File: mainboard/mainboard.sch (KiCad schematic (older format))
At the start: 107 parts, among them J1 USB_B_Micro, J2 Conn_01x19_MountingPin, J3 Conn_01x19_MountingPin, J4 Conn_01x02_Male, Q1 DMG2301L, Q2 MMBT3904, Q3 MMBT3904, SW1 SW_Push, SW2 SW_Push, U1 ESP32-WROOM-32, U2 tps63070, U3 tps63070, U4 tps63070, U5 CP2102N-A01-GQFN24, U6 BME680, U7 BH1750FVI, U8 LIS3MDL, U9 ADXL343

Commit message: Connect XT30 mounting pins to ground
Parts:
- removed J4: Conn_01x02_Male, mainboard:XT30PW, symbol Connector:Conn_01x02_Male
- added J?: Conn_01x02_MountingPin, mainboard:XT30PW, symbol Connector_Generic_MountingPin:Conn_01x02_MountingPin
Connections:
- wire segments 578 -> 582
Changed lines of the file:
@@
 Wire Wire Line
 	14550 4750 14550 4600
-$Comp
-L Connector:Conn_01x02_Male J4
-U 1 1 5DFAE882
-P 13750 4750
-F 0 "J4" H 13858 4931 50  0000 C CNN
-F 1 "Conn_01x02_Male" H 13858 4840 50  0000 C CNN
-F 2 "mainboard:XT30PW" H 13750 4750 50  0001 C CNN
-F 3 "~" H 13750 4750 50  0001 C CNN
-	1    13750 4750
-	1    0    0    -1
-$EndComp
 Wire Wire Line
 	13950 4750 14150 4750
@@
 	14550 5050 14550 4850
 Wire Wire Line
-	14550 4850 13950 4850
+	14550 4850 14000 4850
 Wire Notes Line
 	13450 3900 13450 5300
@@
 Wire Wire Line
 	8800 9500 8800 9100
-Wire Bus Line
-	8350 2150 8350 2500
-Wire Bus Line
-	9350 2500 9350 2750
 Connection ~ 8800 9100
 Wire Wire Line
@@
 	0    -1   -1   0
 $EndComp
+$Comp
+L Connector_Generic_MountingPin:Conn_01x02_MountingPin J?
+U 1 1 5F516B43
+P 13750 4750
+F 0 "J?" H 13672 4967 50  0000 C CNN
+F 1 "Conn_01x02_MountingPin" H 13672 4876 50  0000 C CNN
+F 2 "mainboard:XT30PW" H 13750 4750 50  0001 C CNN
+F 3 "~" H 13750 4750 50  0001 C CNN
+	1    13750 4750
+	-1   0    0    -1
+$EndComp
+Wire Wire Line
+	13750 5050 13750 5100
+Wire Wire Line
+	13750 5100 14000 5100
+Wire Wire Line
+	14000 5100 14000 4850
+Wire Bus Line
+	8350 2150 8350 2500
+Wire Bus Line
+	9350 2500 9350 2750
+Connection ~ 14000 4850
+Wire Wire Line
+	14000 4850 13950 4850
 $EndSCHEMATC

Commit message: Reassign silkscreen designators
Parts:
- gave numbers to parts that had none: 1
- renumbered C38 to C25, C39 to C26, C28 to C27, C29 to C28, C41 to C29, C42 to C32, C40 to C33, C44 to C34, C25 to C35, C43 to C36, C36 to C37, C37 to C38, C26 to C39, C27 to C40, C32 to C41, C33 to C42, C34 to C43, C35 to C44, D2 to D1, D1 to D2, F4 to F3, J2 to J3, J3 to J4, JP4 to JP1, R11 to R1, R8 to R10, R9 to R11, R10 to R12, R15 to R13, R16 to R14, R17 to R15, R18 to R16, R19 to R17, R20 to R18, R13 to R19, R12 to R2, R14 to R20, R1 to R3, R2 to R4, R3 to R5, R4 to R6, R5 to R7, R6 to R8, R7 to R9, U3 to U1, U4 to U3, U6 to U4, U8 to U5, U7 to U6, U5 to U7, U1 to U8

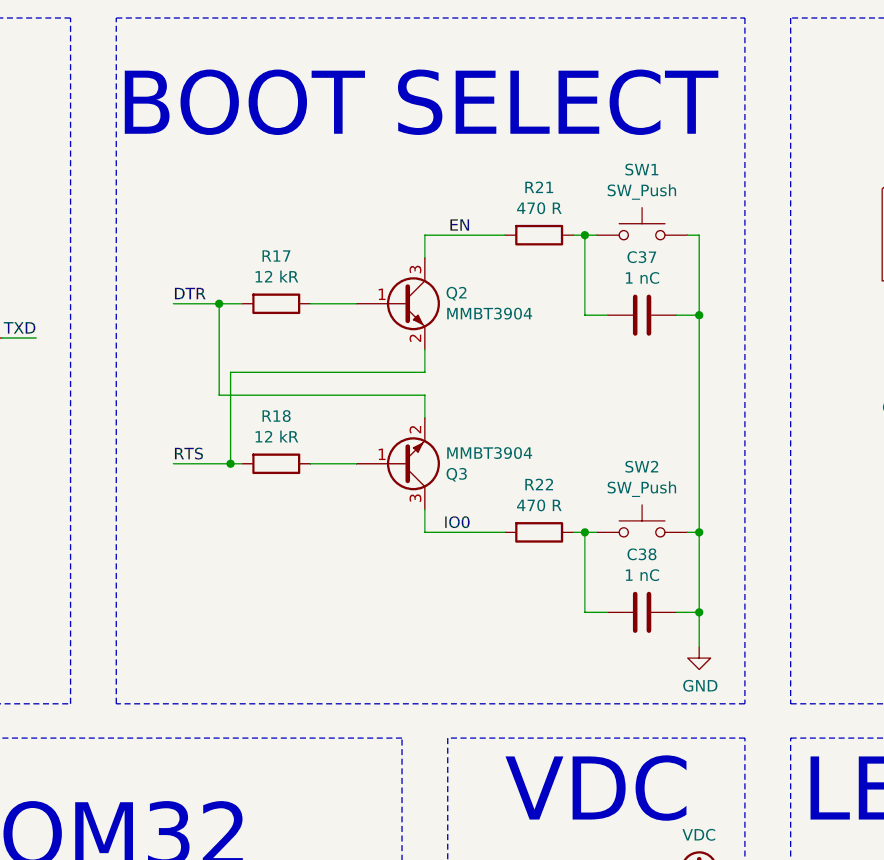
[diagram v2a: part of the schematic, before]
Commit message: Replace reset circuitry
It was the reference circuit used on the DevKitC V4 but it just plain does not work.
Replaced by much simpler and more reliable design.
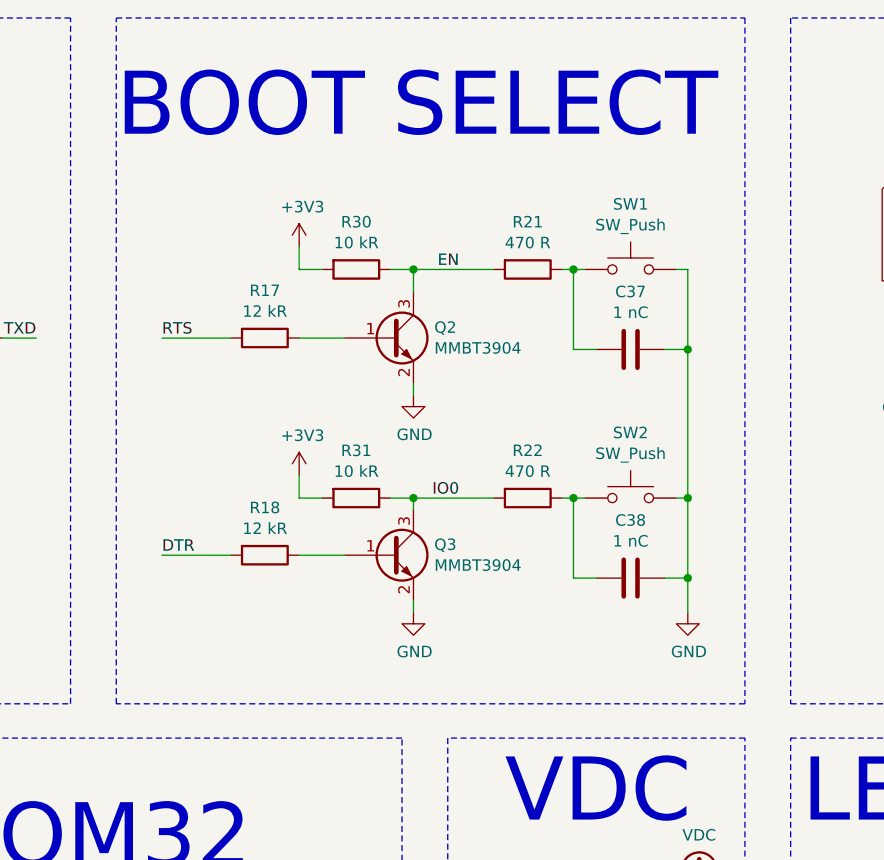
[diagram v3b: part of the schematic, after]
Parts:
- added R30, R31: 10 kR, Resistor_SMD:R_0805_2012Metric, symbol Device:R
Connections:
- net +3V3: now also R30.2, R31.2
- net DTR: now also R18.2; no longer Q3.2 (E), R17.2
- net EN: now also R30.1
- net GND: now also Q2.2 (E), Q3.2 (E)
- net IO0: now also R31.1
- net RTS: now also R17.2; no longer Q2.2 (E), R18.2
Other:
- moved on the sheet: C37, C38, Q2, Q3, R17, R18, R21, R22, SW1, SW2

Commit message: Revert "Replace reset circuitry"
This reverts commit 4aa51ba1305b71722c80cb68cdfb79191ae487c4.

CP2102N defaults to RTS + CTS high. Thus the reference reset circuitry is the only
simple way to make this work
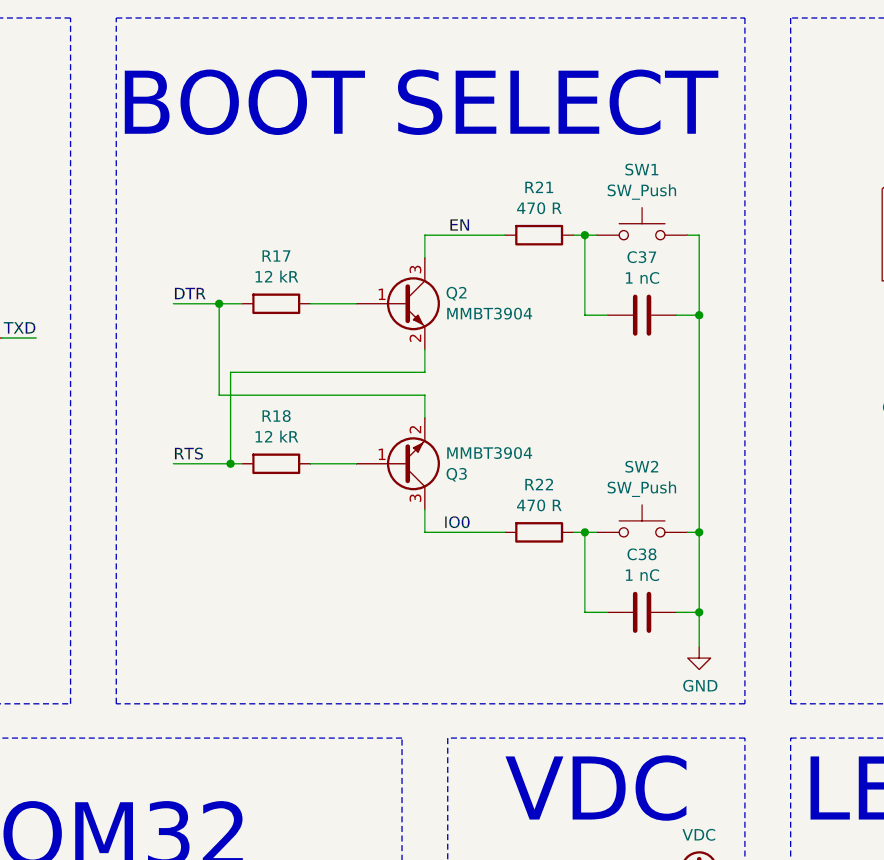
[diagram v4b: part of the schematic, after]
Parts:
- removed R30, R31: 10 kR, Resistor_SMD:R_0805_2012Metric, symbol Device:R
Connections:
- net DTR: now also Q3.2 (E), R17.2; no longer R18.2
- net GND: no longer Q2.2 (E), Q3.2 (E)
- net RTS: now also Q2.2 (E), R18.2; no longer R17.2
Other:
- moved on the sheet: C37, C38, Q2, Q3, R17, R18, R21, R22, SW1, SW2

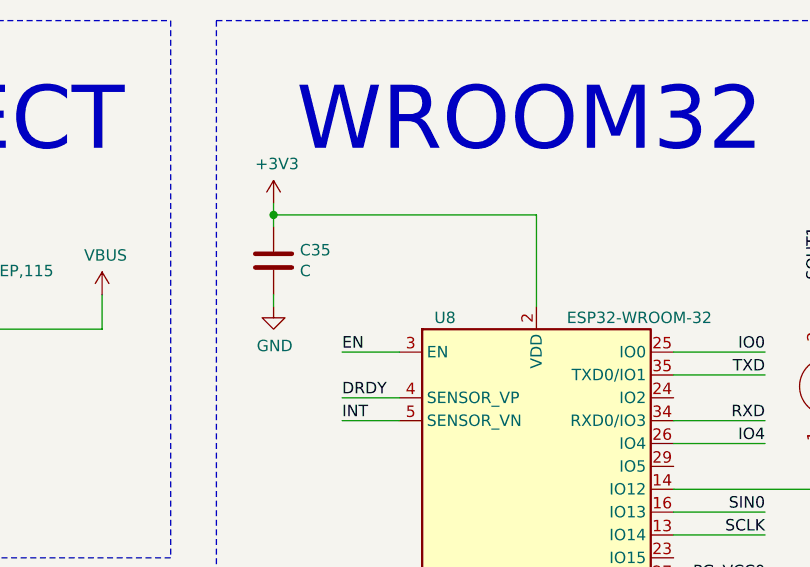
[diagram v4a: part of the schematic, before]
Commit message: Add ~RESET pullup
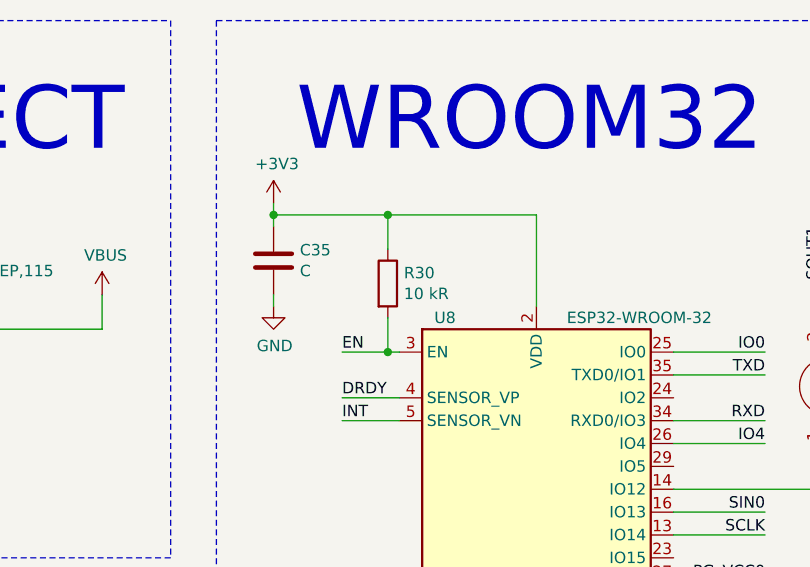
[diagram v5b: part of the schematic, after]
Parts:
- added R30: 10 kR, Resistor_SMD:R_0805_2012Metric, symbol Device:R
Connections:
- net +3V3: now also R30.1
- net EN: now also R30.2
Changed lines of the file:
@@
 $EndComp
-Wire Wire Line
-	14550 3500 14550 3350
-Connection ~ 14550 3350
 Wire Wire Line
 	14550 3000 14550 2050
@@
 	12250 2700 12500 2700
 Wire Wire Line
-	11000 5350 10750 5350
+	11000 5350 10950 5350
 Text Label 10750 5350 0    50   ~ 0
 EN
@@
 	11600 5150 11600 4750
 Wire Wire Line
-	11600 4750 10450 4750
+	11600 4750 10950 4750
 Connection ~ 10450 4750
 Wire Wire Line
@@
 Wire Wire Line
 	14000 5100 14000 4850
+Connection ~ 14000 4850
+Wire Wire Line
+	14000 4850 13950 4850
+Connection ~ 14550 3350
+Wire Wire Line
+	14550 3500 14550 3350
+$Comp
+L Device:R R30
+U 1 1 5D42A7B3
+P 10950 5050
+F 0 "R30" H 11020 5096 50  0000 L CNN
+F 1 "10 kR" H 11020 5005 50  0000 L CNN
+F 2 "Resistor_SMD:R_0805_2012Metric" V 10880 5050 50  0001 C CNN
+F 3 "~" H 10950 5050 50  0001 C CNN
+	1    10950 5050
+	1    0    0    -1
+$EndComp
+Wire Wire Line
+	10950 5200 10950 5350
+Connection ~ 10950 5350
+Wire Wire Line
+	10950 5350 10750 5350
+Wire Wire Line
+	10950 4900 10950 4750
 Wire Bus Line
 	8350 2150 8350 2500
 Wire Bus Line
 	9350 2500 9350 2750
-Connection ~ 14000 4850
-Wire Wire Line
-	14000 4850 13950 4850
+Connection ~ 10950 4750
+Wire Wire Line
+	10950 4750 10450 4750
 $EndSCHEMATC

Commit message: Add WROOM-32 with GND pad
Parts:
- U8: symbol RF_Module:ESP32-WROOM-32 -> esp32-wroom-32_gnd_pad:ESP32-WROOM-32
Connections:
- net GND: now also U8.39 (GND)
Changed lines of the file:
@@
 $EndDescr
 $Comp
-L RF_Module:ESP32-WROOM-32 U8
+L esp32-wroom-32_gnd_pad:ESP32-WROOM-32 U8
 U 1 1 5CF907D7
 P 11600 6550
@@
 Wire Wire Line
 	10950 4900 10950 4750
+Connection ~ 10950 4750
+Wire Wire Line
+	10950 4750 10450 4750
 Wire Bus Line
 	8350 2150 8350 2500
 Wire Bus Line
 	9350 2500 9350 2750
-Connection ~ 10950 4750
-Wire Wire Line
-	10950 4750 10450 4750
 $EndSCHEMATC

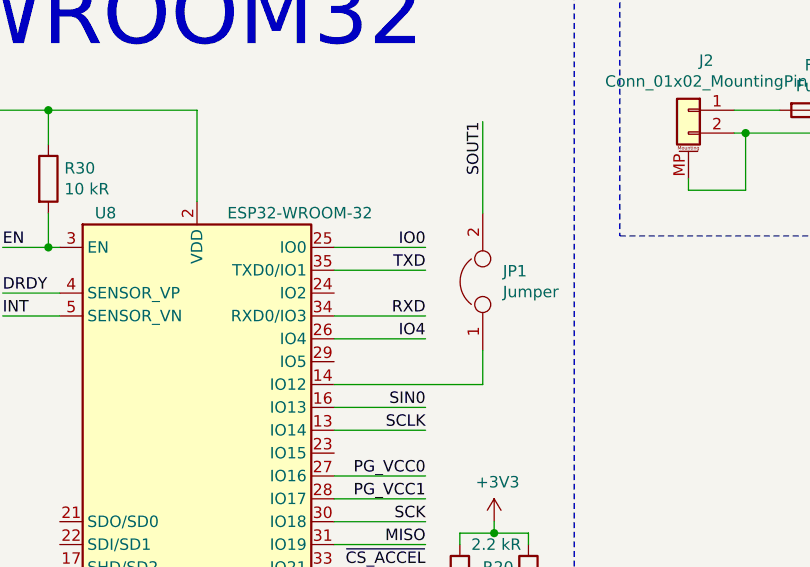
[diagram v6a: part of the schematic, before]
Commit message: Swap RXD and TXD
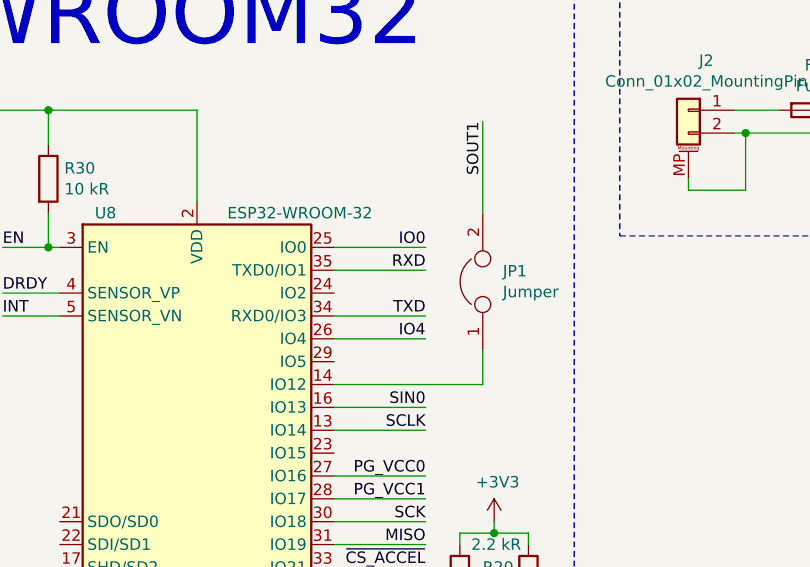
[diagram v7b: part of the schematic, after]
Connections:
- net RXD: now also U8.35 (TXD0/IO1); no longer U8.34 (RXD0/IO3)
- net TXD: now also U8.34 (RXD0/IO3); no longer U8.35 (TXD0/IO1)
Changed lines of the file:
@@
 Wire Wire Line
 	12200 5650 12600 5650
+Text Label 12600 5650 2    50   ~ 0
+TXD
 Text Label 12600 5450 2    50   ~ 0
-TXD
-Text Label 12600 5650 2    50   ~ 0
 RXD
 $Comp

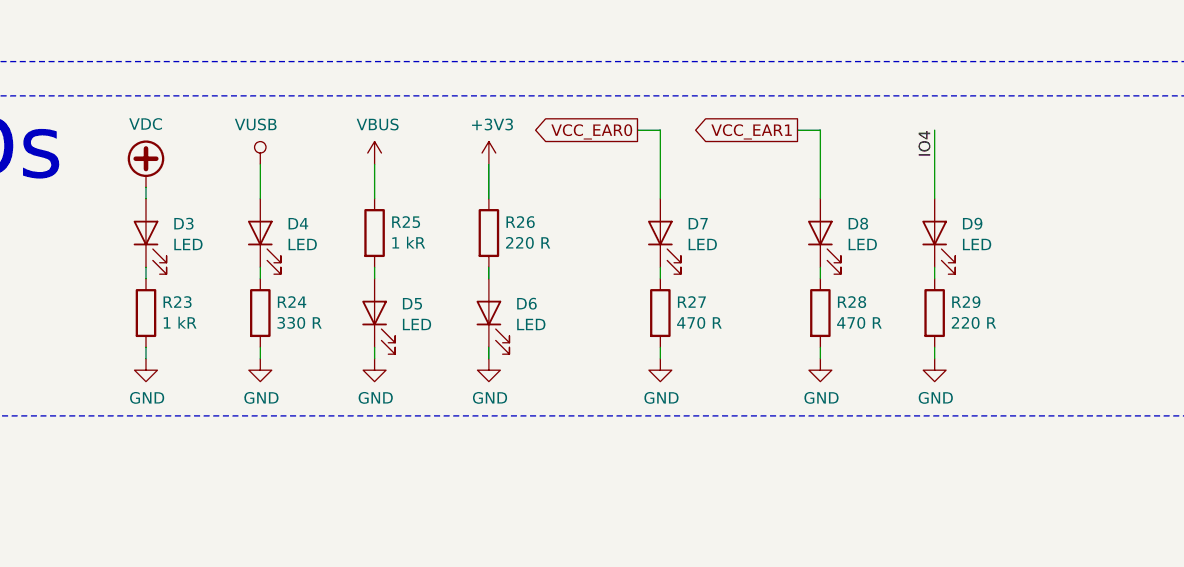
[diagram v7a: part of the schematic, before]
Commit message: Adjust LED resistors for less eye piercing brightness
Green LEDs really are bright. Reduce current to ~300 µA
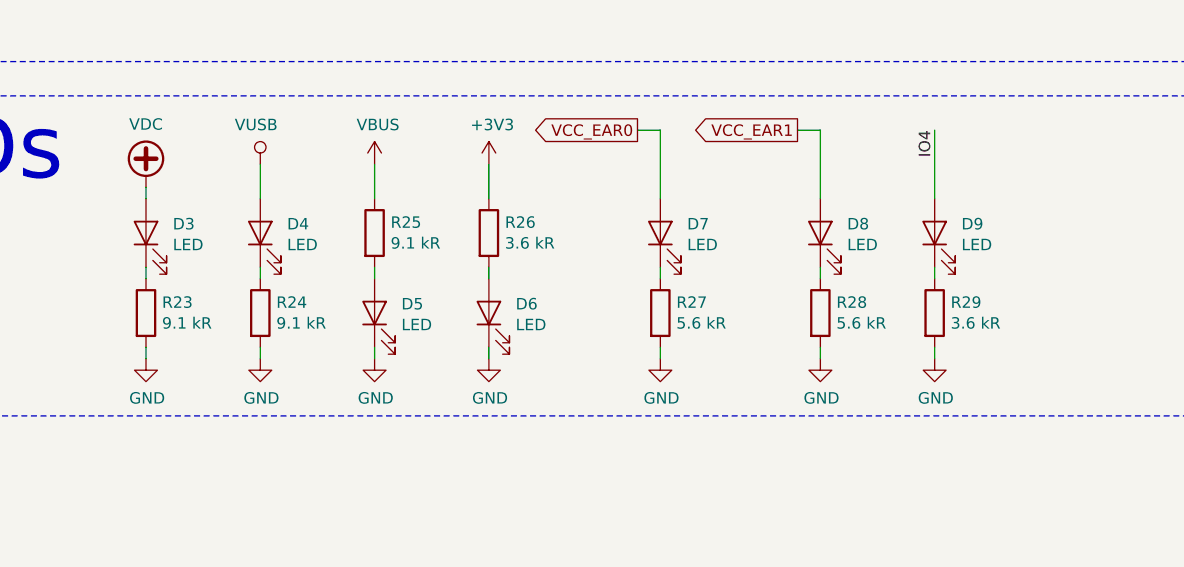
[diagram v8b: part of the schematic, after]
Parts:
- R23, R25: value 1 kR -> 9.1 kR
- R24: value 330 R -> 9.1 kR
- R26, R29: value 220 R -> 3.6 kR
- R27, R28: value 470 R -> 5.6 kR
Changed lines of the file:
@@
 P 16300 4850
 F 0 "R23" H 16370 4896 50  0000 L CNN
-F 1 "1 kR" H 16370 4805 50  0000 L CNN
+F 1 "9.1 kR" H 16370 4805 50  0000 L CNN
 F 2 "Resistor_SMD:R_0805_2012Metric" V 16230 4850 50  0001 C CNN
 F 3 "~" H 16300 4850 50  0001 C CNN
@@
 P 16800 4850
 F 0 "R24" H 16870 4896 50  0000 L CNN
-F 1 "330 R" H 16870 4805 50  0000 L CNN
+F 1 "9.1 kR" H 16870 4805 50  0000 L CNN
 F 2 "Resistor_SMD:R_0805_2012Metric" V 16730 4850 50  0001 C CNN
 F 3 "~" H 16800 4850 50  0001 C CNN
@@
 P 17300 4500
 F 0 "R25" H 17370 4546 50  0000 L CNN
-F 1 "1 kR" H 17370 4455 50  0000 L CNN
+F 1 "9.1 kR" H 17370 4455 50  0000 L CNN
 F 2 "Resistor_SMD:R_0805_2012Metric" V 17230 4500 50  0001 C CNN
 F 3 "~" H 17300 4500 50  0001 C CNN
@@
 P 18550 4850
 F 0 "R27" H 18620 4896 50  0000 L CNN
-F 1 "470 R" H 18620 4805 50  0000 L CNN
+F 1 "5.6 kR" H 18620 4805 50  0000 L CNN
 F 2 "Resistor_SMD:R_0805_2012Metric" V 18480 4850 50  0001 C CNN
 F 3 "~" H 18550 4850 50  0001 C CNN
@@
 P 19250 4850
 F 0 "R28" H 19320 4896 50  0000 L CNN
-F 1 "470 R" H 19320 4805 50  0000 L CNN
+F 1 "5.6 kR" H 19320 4805 50  0000 L CNN
 F 2 "Resistor_SMD:R_0805_2012Metric" V 19180 4850 50  0001 C CNN
 F 3 "~" H 19250 4850 50  0001 C CNN
@@
 P 19750 4850
 F 0 "R29" H 19820 4896 50  0000 L CNN
-F 1 "220 R" H 19820 4805 50  0000 L CNN
+F 1 "3.6 kR" H 19820 4805 50  0000 L CNN
 F 2 "Resistor_SMD:R_0805_2012Metric" V 19680 4850 50  0001 C CNN
 F 3 "~" H 19750 4850 50  0001 C CNN
@@
 P 17800 4500
 F 0 "R26" H 17870 4546 50  0000 L CNN
-F 1 "220 R" H 17870 4455 50  0000 L CNN
+F 1 "3.6 kR" H 17870 4455 50  0000 L CNN
 F 2 "Resistor_SMD:R_0805_2012Metric" V 17730 4500 50  0001 C CNN
 F 3 "~" H 17800 4500 50  0001 C CNN
